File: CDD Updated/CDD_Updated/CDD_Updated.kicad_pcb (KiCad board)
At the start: 4 copper layers, 34.3 x 25.7 mm, 5 parts, among them U3 MOUDLE-SEEEDUINO-XIAO-ESP32C3

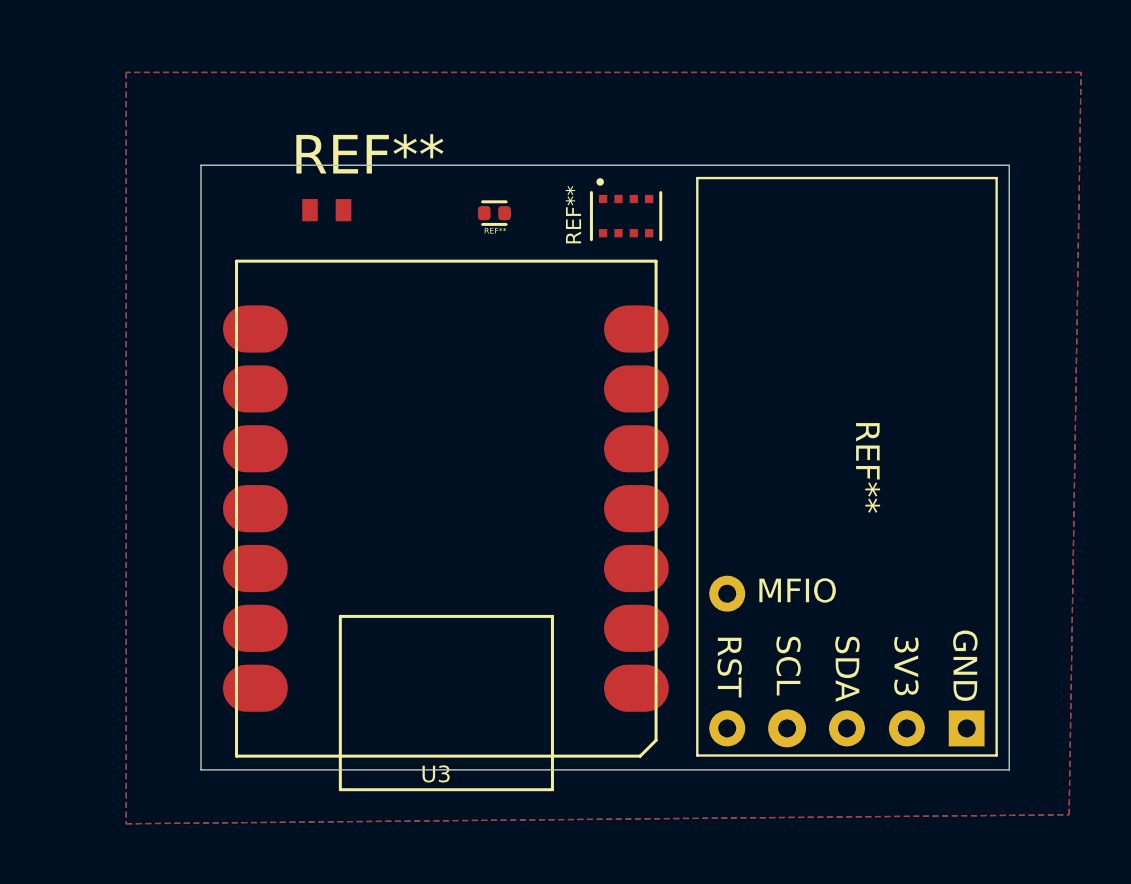
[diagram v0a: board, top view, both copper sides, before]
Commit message: Update KiCAD files and route PCB
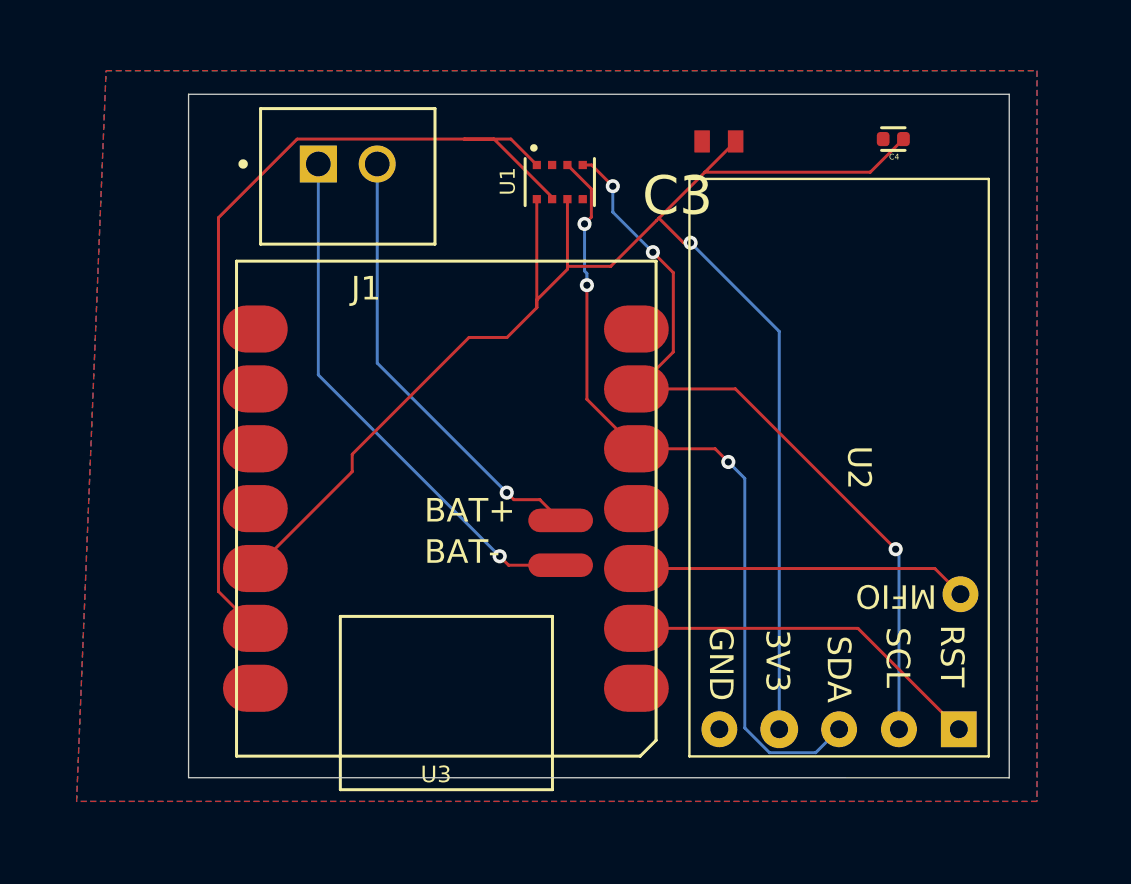
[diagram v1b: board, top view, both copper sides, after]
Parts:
- removed REF**: CAPC1005X55N_0.1NF, CDD Updated:CAPC1005X55N_0.1NF
- removed REF**: MAX30101_PPG_Sensor, CDD Updated:MAX30101_PPG_Sensor
- removed REF**: CAPC1608X90N_47uF, CDD Updated:CAPC1608X90N_47uF
- removed REF**: XDCR_DPS368XTSA1, CDD Updated:XDCR_DPS368XTSA1_Pressure_Sensor
- added C3: CL10A475KP8NNNC, CDD Updated:CAPC1608X90N_47uF, F.Cu at (127.0, 79.0)
- added C4: CL05B104KP5NNNC, CDD Updated:CAPC1005X55N_0.1NF, F.Cu at (134.4, 78.9)
- added J1: B2B-XH-A, CDD Updated:JST_B2B-XH-A, F.Cu at (111.3, 80.5)
- added U1: DPS368XTSA1_PRESSURE_SENSOR, CDD Updated:XDCR_DPS368XTSA1_Pressure_Sensor, F.Cu at (120.2, 80.7)
- added U2: MAX30101, CDD Updated:MAX30101_PPG_Sensor, F.Cu at (125.8, 105.2)
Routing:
- net /3V3: track 0.00 -> 69.0 mm, vias 0 -> 1
- net GND: track 0.00 -> 38.2 mm
- net /SDA: track 0.00 -> 34.0 mm, vias 0 -> 3
- net /SCK: track 0.00 -> 33.5 mm, vias 0 -> 3
- net Net-(U3-BAT_-): track 0.00 -> 22.6 mm, vias 0 -> 1
- net Net-(U3-BAT_+): track 0.00 -> 19.0 mm, vias 0 -> 1
- net /RST: track 0.00 -> 15.5 mm
- net /MFIO: track 0.00 -> 14.2 mm
- removed copper zone on In1.Cu, net GND
- removed copper zone on In2.Cu, net GND
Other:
- board size 34.3 x 25.7 mm -> 34.8 x 29 mm

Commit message: Update PCB
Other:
- board size 34.8 x 29 mm -> 34.8 x 29.8 mm
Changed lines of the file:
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@@
 		(at 127 79 180)
 		(property "Reference" "C3"
-			(at 1.7526 -2.3114 360)
+			(at 3.4 -0.3 0)
 			(layer "F.SilkS")
 			(effects
@@
 			(at 9.0424 2.1336 90)
 			(layer "F.Fab")
+			(hide yes)
 			(effects
 				(font
@@
 		)
 		(property "Footprint" "CDD Updated:CAPC1608X90N_47uF"
-			(at 0 0 360)
+			(at 0 0 0)
 			(layer "F.Fab")
 			(hide yes)
@@
 		)
 		(property "Datasheet" ""
-			(at 0 0 360)
+			(at 0 0 0)
 			(layer "F.Fab")
 			(hide yes)
@@
 		)
 		(property "Description" ""
-			(at 0 0 360)
+			(at 0 0 0)
 			(layer "F.Fab")
 			(hide yes)
@@
 		(at 111.2552 80.4826 180)
 		(property "Reference" "J1"
-			(at -0.775 -4.76 360)
+			(at -0.775 -4.76 0)
 			(layer "F.SilkS")
 			(effects
@@
 		)
 		(property "Value" "B2B-XH-A"
-			(at 3.67 4.76 360)
-			(layer "F.Fab")
+			(at 3.67 4.76 0)
+			(layer "F.Fab")
+			(hide yes)
 			(effects
 				(font
@@
 		)
 		(property "Footprint" "CDD Updated:JST_B2B-XH-A"
-			(at 0 0 360)
+			(at 0 0 0)
 			(layer "F.Fab")
 			(hide yes)
@@
 		)
 		(property "Datasheet" ""
-			(at 0 0 360)
+			(at 0 0 0)
 			(layer "F.Fab")
 			(hide yes)
@@
 		)
 		(property "Description" ""
-			(at 0 0 360)
+			(at 0 0 0)
 			(layer "F.Fab")
 			(hide yes)
@@
 			(at 9.3345 -21.7805 0)
 			(layer "F.SilkS")
+			(hide yes)
 			(effects
 				(font
@@
 		(attr through_hole)
 		(fp_line
-			(start 17.8 0)
-			(end 17.8 -21)
+			(start 18.75 0)
+			(end 18.75 -21)
 			(stroke
 				(width 0.127)
@@
 		)
 		(fp_line
-			(start 0 -20.3285)
-			(end 0 0)
+			(start -1 -20.3285)
+			(end -1 0)
 			(stroke
 				(width 0.127)
@@
 			(at 0.032 -2.2064 90)
 			(layer "F.SilkS")
+			(hide yes)
 			(effects
 				(font
@@
 		(sheetname "Root")
 		(sheetfile "CDD_Updated.kicad_sch")
-		(attr smd)
+		(attr smd allow_soldermask_bridges)
 		(fp_circle
 			(center 0.725 -0.975)
@@
 		(at 134.4 78.9 180)
 		(property "Reference" "C4"
-			(at -0.038171 -0.755633 360)
-			(layer "F.SilkS")
+			(at -0.038171 -0.755633 0)
+			(layer "F.SilkS")
+			(hide yes)
 			(effects
 				(font
 					(size 0.241029 0.241029)
-					(thickness 0.15)
+					(thickness 0.060257)
 				)
 			)
 		)
 		(property "Value" "CL05B104KP5NNNC"
-			(at 1.032975 0.851042 360)
-			(layer "F.Fab")
+			(at 1.032975 0.851042 0)
+			(layer "F.Fab")
+			(hide yes)
 			(effects
 				(font
 					(size 0.240973 0.240973)
-					(thickness 0.15)
+					(thickness 0.060243)
 				)
 			)
 		)
 		(property "Footprint" "CDD Updated:CAPC1005X55N_0.1NF"
-			(at 0 0 360)
+			(at 0 0 0)
 			(layer "F.Fab")
 			(hide yes)
@@
 		)
 		(property "Datasheet" ""
-			(at 0 0 360)
+			(at 0 0 0)
 			(layer "F.Fab")
 			(hide yes)
@@
 		)
 		(property "Description" ""
-			(at 0 0 360)
+			(at 0 0 0)
 			(layer "F.Fab")
 			(hide yes)
@@
 		(sheetname "Root")
 		(sheetfile "CDD_Updated.kicad_sch")
-		(attr smd)
+		(attr smd allow_soldermask_bridges)
 		(fp_line
 			(start 0.5 -0.48)
@@
 	(gr_line
 		(start 104.5 77)
-		(end 104.5 105.995)
+		(end 104.4905 106.7975)
 		(stroke
 			(width 0.0381)
@@
 	)
 	(gr_line
-		(start 139.319 106)
+		(start 139.3095 106.8025)
 		(end 139.319 77)
 		(stroke
@@
 	)
 	(gr_line
-		(start 104.5 105.995)
-		(end 139.319 106)
+		(start 104.4905 106.7975)
+		(end 139.3095 106.8025)
 		(stroke
 			(width 0.0381)

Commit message: Update PCB
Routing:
- net GND: track 38.2 -> 9.23 mm
- net /3V3: track 69.0 -> 83.3 mm
- net /SDA: track 34.0 -> 31.1 mm, vias 3 -> 1
- net /RST: track 15.5 -> 17.0 mm
- net Net-(U3-BAT_-): track 22.6 -> 21.3 mm, vias 1 -> 0
- net Net-(U3-BAT_+): track 19.0 -> 19.4 mm, vias 1 -> 0
- net /SCK: track 33.5 -> 33.2 mm, vias 3 -> 1

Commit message: update pcb and schematic - remove extra sensors
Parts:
- removed C3: CL10A475KP8NNNC, CDD Updated:CAPC1608X90N_47uF
- removed C4: CL05B104KP5NNNC, CDD Updated:CAPC1005X55N_0.1NF
- removed U1: DPS368XTSA1_PRESSURE_SENSOR, CDD Updated:XDCR_DPS368XTSA1_Pressure_Sensor
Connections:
- net GND renamed /GND
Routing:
- net /3V3: track 83.3 -> 29.5 mm
- net /SDA: track 31.1 -> 17.9 mm
- net /SCK: track 33.2 -> 21.5 mm
- net /GND: track 9.23 -> 0.00 mm

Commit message: optimized pcb for size
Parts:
- J1, U3: moved to B.Cu
- moved J1 24.0 mm to (120.8, 102.5), turned to 0 degrees
- moved U3 18.1 mm to (134.3, 99.1)
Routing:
- net /GND: track 0.00 -> 39.1 mm
- net /RST: track 17.0 -> 26.3 mm
- net /SCK: track 21.5 -> 13.2 mm, vias 1 -> 0
- net Net-(U3-BAT_-): track 21.3 -> 24.3 mm, vias 0 -> 1
- net /SDA: track 17.9 -> 15.2 mm, vias 1 -> 0
- net /MFIO: track 14.2 -> 15.8 mm
- net Net-(U3-BAT_+): track 19.4 -> 20.6 mm, vias 0 -> 1
- net /3V3: track 29.5 -> 29.2 mm, vias 1 -> 0
- removed copper zone on B.Cu, net /GND
- removed copper zone on F.Cu, net /GND
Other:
- board size 34.8 x 29.8 mm -> 24.8 x 30.3 mm

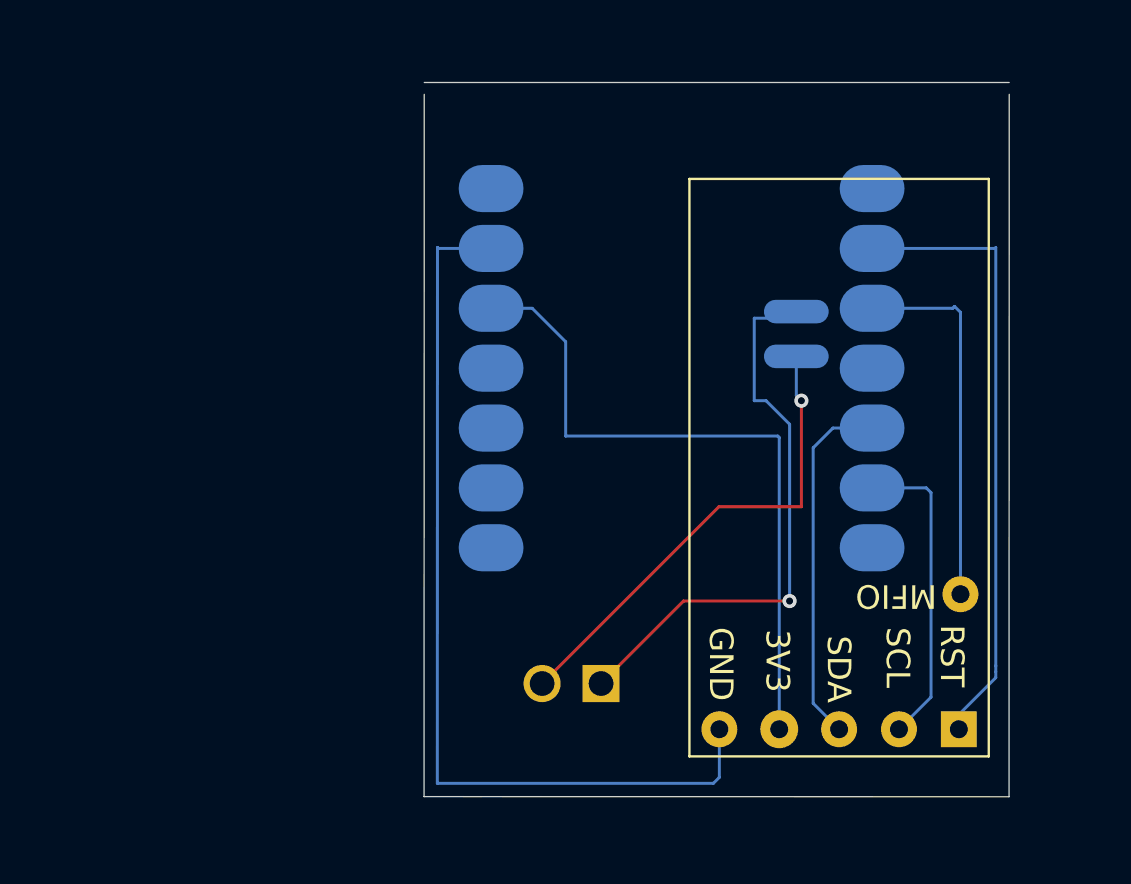
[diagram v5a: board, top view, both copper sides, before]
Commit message: fixed routing error
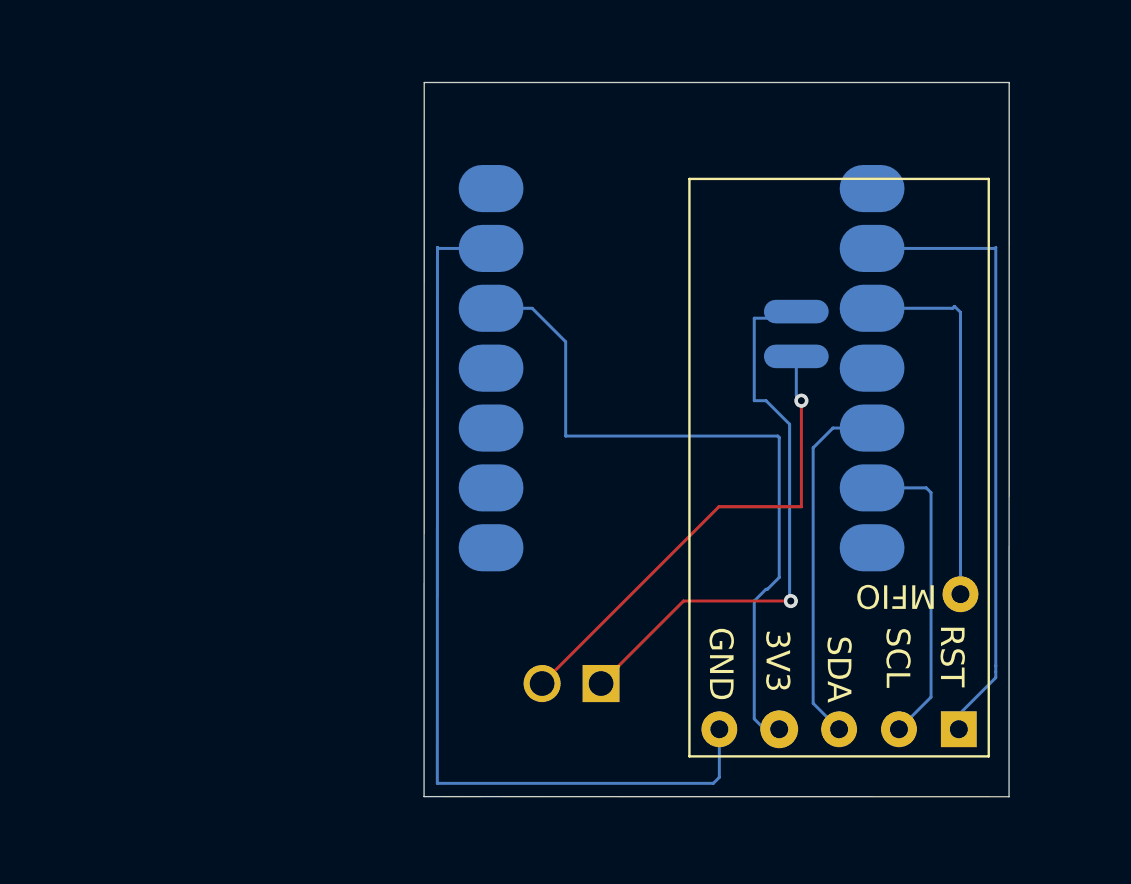
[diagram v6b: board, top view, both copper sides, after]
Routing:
- net /3V3: track 29.2 -> 30.5 mm
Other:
- outline, holes or cut-outs redrawn
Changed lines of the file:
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@@
 	)
 	(gr_line
-		(start 114.5 77)
+		(start 114.5 76.5)
 		(end 114.4905 106.7975)
 		(stroke
@@
 	(gr_line
 		(start 139.3095 106.8025)
-		(end 139.319 77)
+		(end 139.319 76.5)
 		(stroke
 			(width 0.0381)
@@
 	)
 	(segment
-		(start 129.56 103.9395)
+		(start 128.5 98.5)
+		(end 128.5 103.5)
+		(width 0.127)
+		(layer "B.Cu")
+		(net "/3V3")
+	)
+	(segment
+		(start 129.56 97.5)
 		(end 129.56 91.56)
+		(width 0.127)
+		(layer "B.Cu")
+		(net "/3V3")
+	)
+	(segment
+		(start 128.5 103.5)
+		(end 128.9395 103.9395)
+		(width 0.127)
+		(layer "B.Cu")
+		(net "/3V3")
+	)
+	(segment
+		(start 128.9395 103.9395)
+		(end 129.56 103.9395)
 		(width 0.127)
 		(layer "B.Cu")
@@
 	)
 	(segment
+		(start 129.56 97.5)
+		(end 129.06 98)
+		(width 0.127)
+		(layer "B.Cu")
+		(net "/3V3")
+	)
+	(segment
+		(start 129.5 91.5)
+		(end 120.5 91.5)
+		(width 0.127)
+		(layer "B.Cu")
+		(net "/3V3")
+	)
+	(segment
 		(start 129.56 91.56)
 		(end 129.5 91.5)
@@
 	)
 	(segment
+		(start 129 98)
+		(end 128.5 98.5)
+		(width 0.127)
+		(layer "B.Cu")
+		(net "/3V3")
+	)
+	(segment
+		(start 120.5 87.5)
+		(end 119.08 86.08)
+		(width 0.127)
+		(layer "B.Cu")
+		(net "/3V3")
+	)
+	(segment
 		(start 119.08 86.08)
 		(end 117.335 86.08)
@@
 	)
 	(segment
-		(start 129.5 91.5)
-		(end 120.5 91.5)
-		(width 0.127)
-		(layer "B.Cu")
-		(net "/3V3")
-	)
-	(segment
-		(start 120.5 87.5)
-		(end 119.08 86.08)
+		(start 129.06 98)
+		(end 129 98)
 		(width 0.127)
 		(layer "B.Cu")
@@
 	)
 	(segment
+		(start 130.0505 98.5)
+		(end 125.5 98.5)
+		(width 0.127)
+		(layer "F.Cu")
+		(net "Net-(U3-BAT_-)")
+	)
+	(segment
 		(start 125.5 98.5)
-		(end 130 98.5)
+		(end 122 102)
 		(width 0.127)
 		(layer "F.Cu")
 		(net "Net-(U3-BAT_-)")
 	)
-	(segment
-		(start 122 102)
-		(end 125.5 98.5)
-		(width 0.127)
-		(layer "F.Cu")
-		(net "Net-(U3-BAT_-)")
-	)
 	(via
-		(at 130 98.5)
+		(at 130.0505 98.5)
 		(size 0.6)
 		(drill 0.3)
@@
 	(segment
 		(start 128.5 90)
+		(end 128.5 86.5)
+		(width 0.127)
+		(layer "B.Cu")
+		(net "Net-(U3-BAT_-)")
+	)
+	(segment
+		(start 128.5 86.5)
+		(end 130.005 86.5)
+		(width 0.127)
+		(layer "B.Cu")
+		(net "Net-(U3-BAT_-)")
+	)
+	(segment
+		(start 130.0505 98.5)
+		(end 130 98.4495)
+		(width 0.127)
+		(layer "B.Cu")
+		(net "Net-(U3-BAT_-)")
+	)
+	(segment
+		(start 130.005 86.5)
+		(end 130.285 86.22)
+		(width 0.127)
+		(layer "B.Cu")
+		(net "Net-(U3-BAT_-)")
+	)
+	(segment
+		(start 130 91)
 		(end 129 90)
 		(width 0.127)
@@
 	(segment
 		(start 129 90)
+		(end 128.5 90)
+		(width 0.127)
+		(layer "B.Cu")
+		(net "Net-(U3-BAT_-)")
+	)
+	(segment
+		(start 130 98.4495)
 		(end 130 91)
 		(width 0.127)
 		(layer "B.Cu")
-		(net "Net-(U3-BAT_-)")
-	)
-	(segment
-		(start 130 91)
-		(end 130 98.5)
-		(width 0.127)
-		(layer "B.Cu")
-		(net "Net-(U3-BAT_-)")
-	)
-	(segment
-		(start 130.005 86.5)
-		(end 128.5 86.5)
-		(width 0.127)
-		(layer "B.Cu")
-		(net "Net-(U3-BAT_-)")
-	)
-	(segment
-		(start 128.5 86.5)
-		(end 128.5 90)
-		(width 0.127)
-		(layer "B.Cu")
-		(net "Net-(U3-BAT_-)")
-	)
-	(segment
-		(start 130.285 86.22)
-		(end 130.005 86.5)
-		(width 0.127)
-		(layer "B.Cu")
